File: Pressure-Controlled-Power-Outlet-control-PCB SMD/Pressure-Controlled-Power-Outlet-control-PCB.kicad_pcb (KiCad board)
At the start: 4 copper layers, 100.3 x 100.3 mm, 47 parts, among them J1 pressure sensor, J2 1017514, J3 I2C0 Connector, J4 SPI1 Connector, J5 FanA 5V/24V, J6 FanB 5V/24V, K1 T9GV5L24-24, K2 T9GV5L24-24, M1 Fan_4pin, M2 Fan_4pin, Q1 2N3906, Q2 IRF540N, Q3 IRF540N, Q4 2N3906, Q5 2N3904, Q6 2N3904, Q7 2N3904, Q8 2N3904, U1 Pico, U2 LM324, U3 LF50_TO220

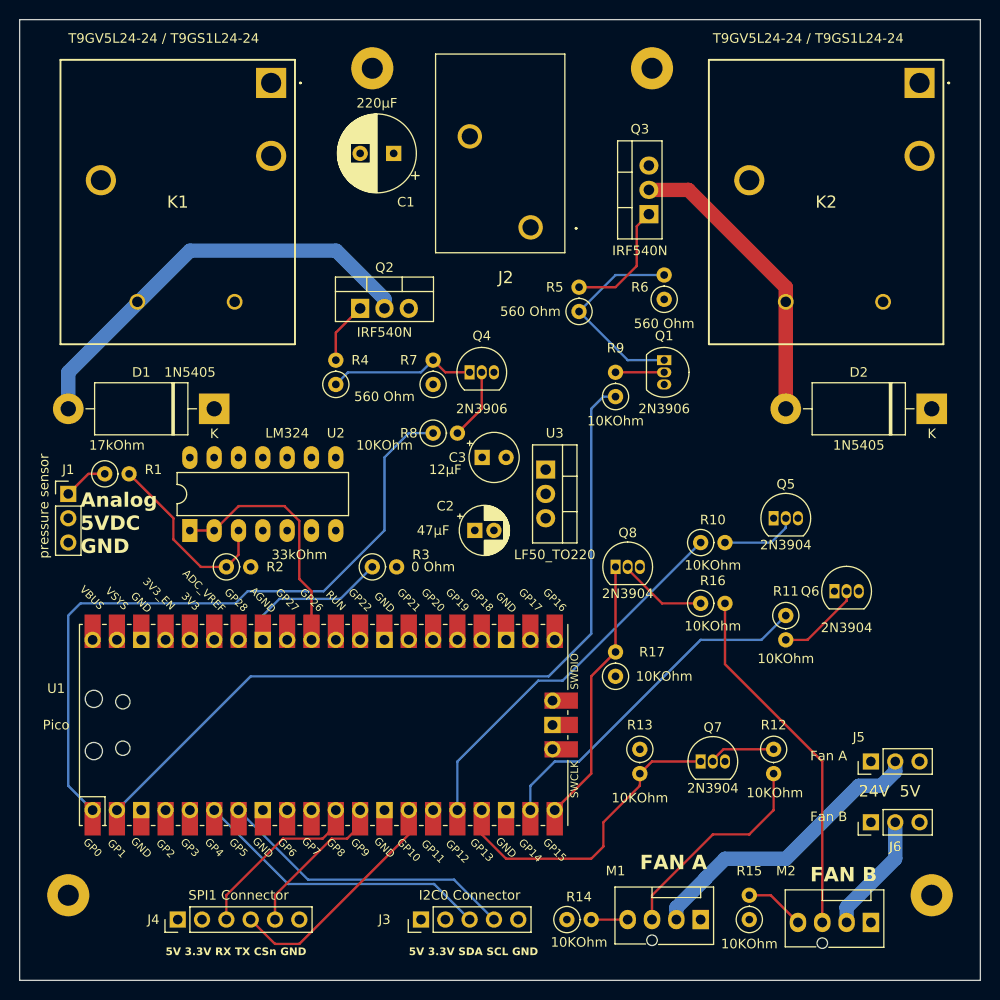
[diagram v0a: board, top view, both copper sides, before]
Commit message: make a quick version that has some SMD for pick and place
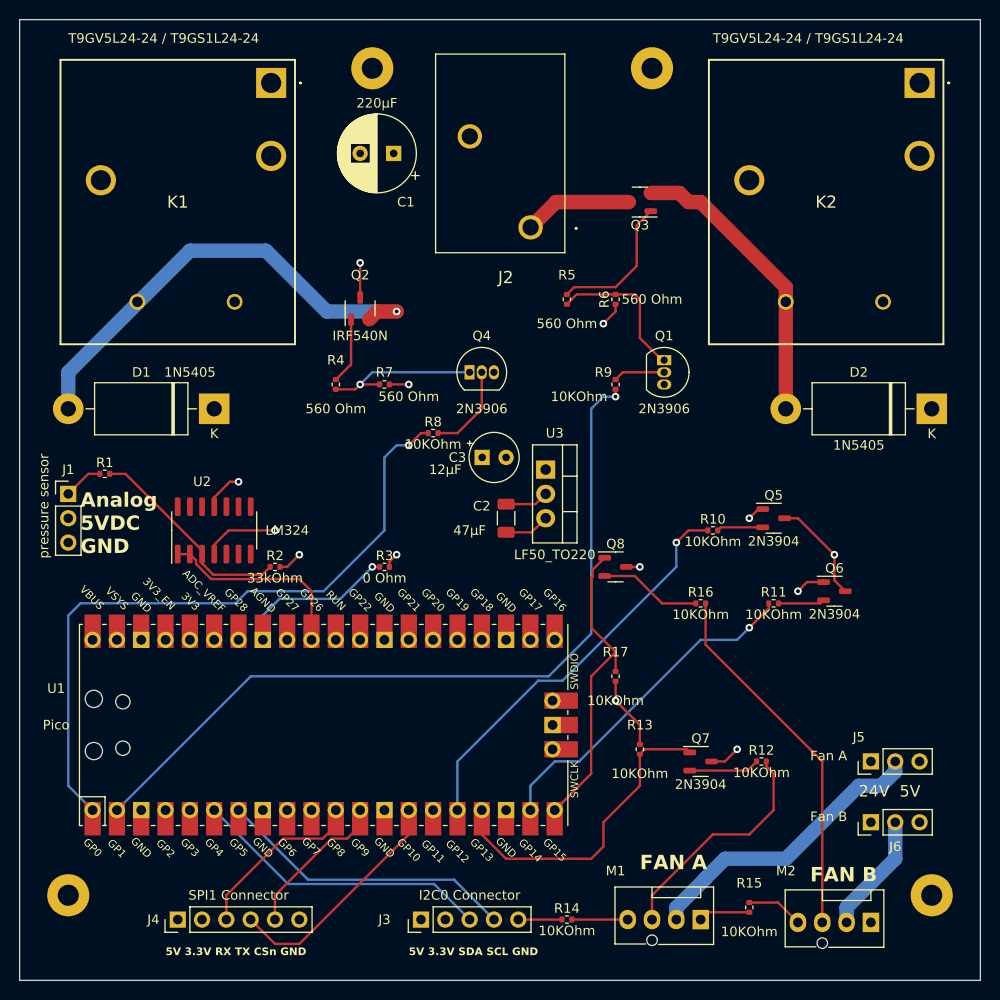
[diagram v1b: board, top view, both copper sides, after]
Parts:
- C2: footprint Capacitor_THT:CP_Radial_D5.0mm_P2.00mm -> Capacitor_SMD:C_1206_3216Metric
- Q2, Q3: footprint Package_TO_SOT_THT:TO-220-3_Vertical -> Package_TO_SOT_SMD:SOT-23-3
- Q5, Q6, Q7, Q8: footprint Package_TO_SOT_THT:TO-92_Inline -> Package_TO_SOT_SMD:SOT-23-3
- R1, R10, R11, R12, R13, R14, R15, R16, R17, R2, R3, R4, R5, R6, R7, R8, R9: footprint Resistor_THT:R_Axial_DIN0207_L6.3mm_D2.5mm_P2.54mm_Vertical -> Resistor_SMD:R_0402_1005Metric
- U2: footprint Package_DIP:DIP-14_W7.62mm_LongPads -> Package_SO:SOIC-14_3.9x8.7mm_P1.27mm
- moved R2 5.08 mm to (113.0, 113.0)
- moved R7 5.08 mm to (124.5, 94.0), turned to 180 degrees
- moved R6 5.08 mm to (148.6, 85.1)
- moved C2 3.51 mm to (137.2, 108.0), turned to 90 degrees
- moved U2 2.55 mm to (106.7, 109.2)
- moved R10 1.80 mm to (158.8, 109.2)
- moved R11 1.80 mm to (165.1, 116.8), turned to 0 degrees
- moved R5 1.80 mm to (143.5, 85.1)
- moved R12 1.80 mm to (163.8, 133.3), turned to 0 degrees
- moved Q3 1.58 mm to (151.1, 74.9), turned to 180 degrees
- moved R15 1.27 mm to (162.6, 148.6)
- moved R3 1.27 mm to (124.5, 113.0)
- moved R9 1.27 mm to (148.6, 94.0)
- turned Q2 to 90 degrees
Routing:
- net GND: track 0.00 -> 50.1 mm, vias 0 -> 7
- net +5V: track 37.4 -> 61.7 mm, vias 0 -> 2
- net Net-(Q1-E): track 21.5 -> 15.8 mm
- net +3.3V: track 140.9 -> 146.4 mm, vias 0 -> 2
- net /ADC0: track 26.1 -> 20.9 mm
- net Net-(M2-PWM): track 41.7 -> 46.8 mm, vias 0 -> 1
- net /FanB_Tac: track 28.0 -> 32.6 mm
- net Net-(Q6-B): track 9.04 -> 4.84 mm
- net Net-(D1-A): track 45.2 -> 49.2 mm, vias 0 -> 1
- net Net-(M1-PWM): track 52.0 -> 55.8 mm, vias 0 -> 1
- net Net-(Q5-B): track 7.99 -> 4.84 mm
- net /FanA_PWM: track 39.9 -> 42.7 mm, vias 0 -> 1
- net Net-(U2A-+): track 19.8 -> 22.3 mm
- net Net-(Q4-B): track 7.40 -> 9.43 mm
- net Net-(Q3-G): track 12.9 -> 14.9 mm
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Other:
- board text removed: "2N3904"
